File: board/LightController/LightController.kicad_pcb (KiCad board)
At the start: 2 copper layers, 79.5 x 67.1 mm, 11 parts, among them J1 Jack-DC, J2 Light bank 1, J3 Light Bank 2, J4 Light Bank 3, U1 CPC1002N, U2 AP63205WU, U3 FeatherS2

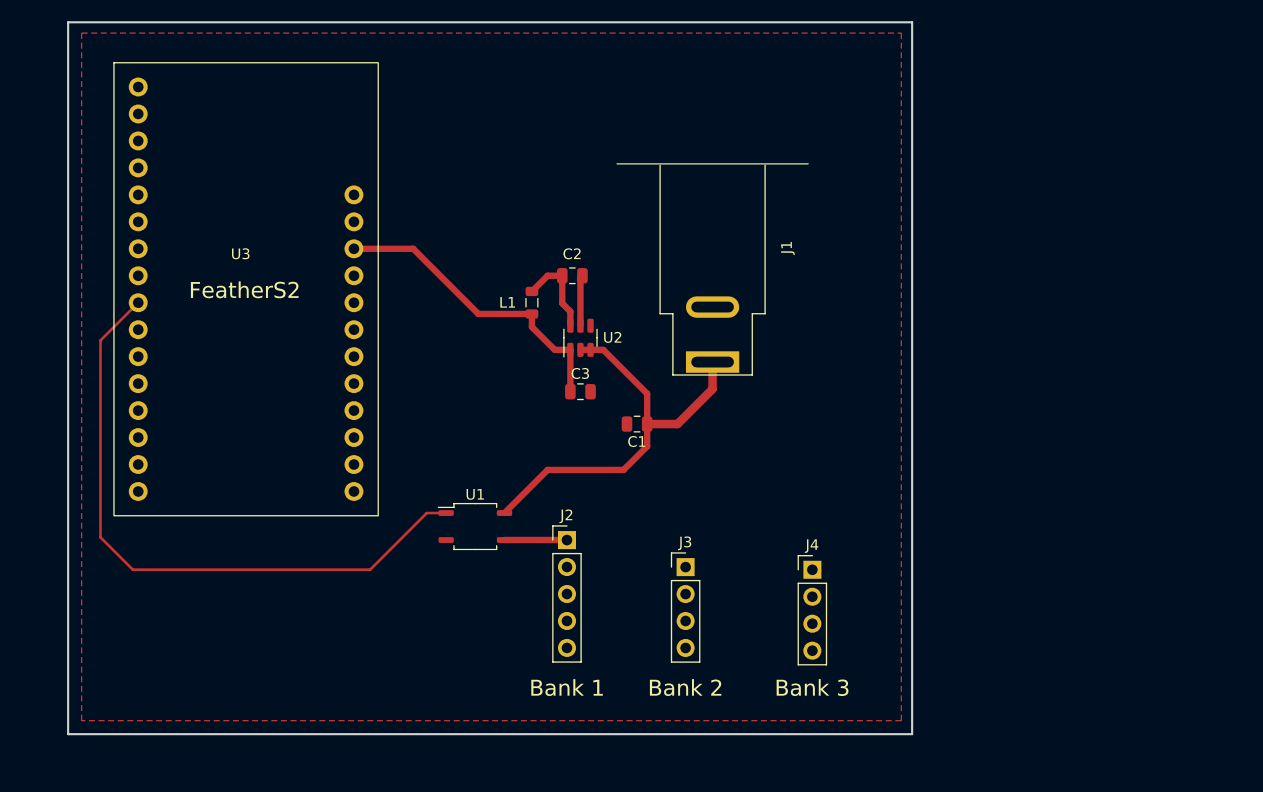
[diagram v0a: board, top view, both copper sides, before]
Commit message: Add mounting holes.
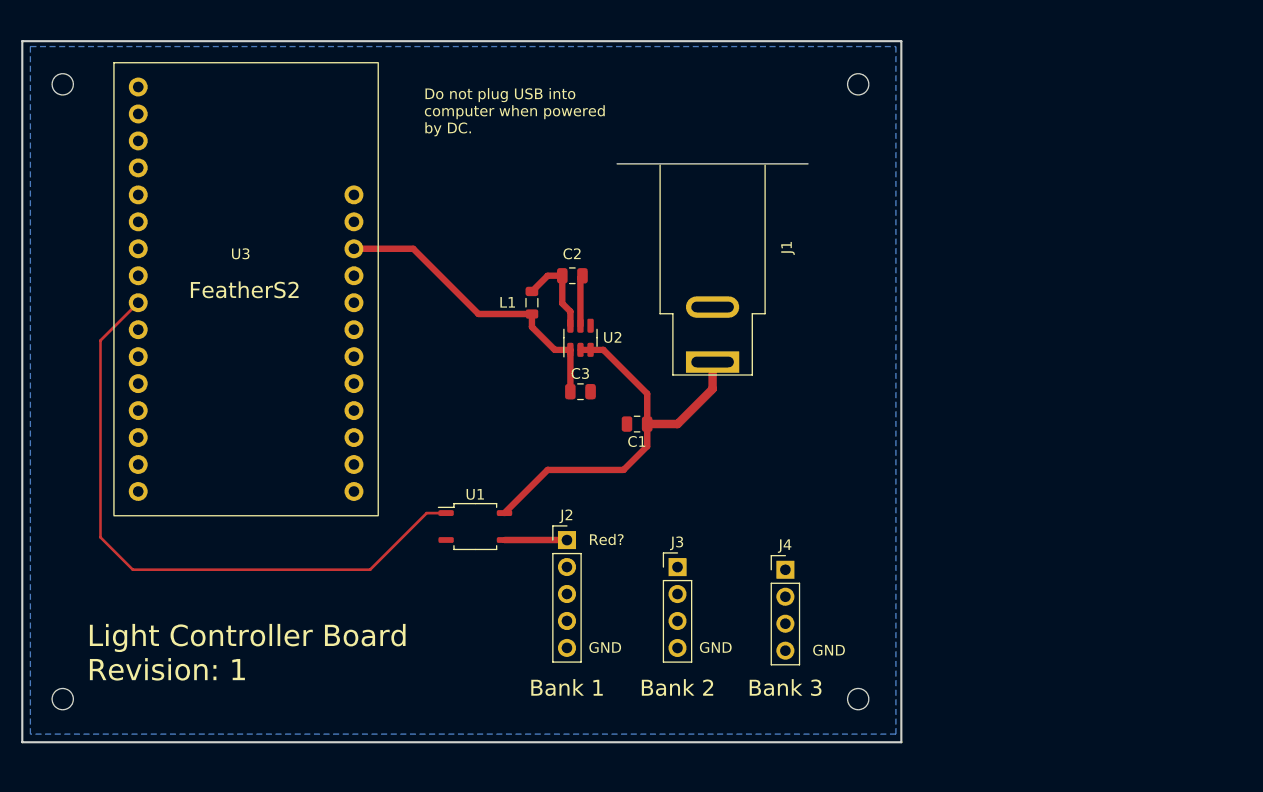
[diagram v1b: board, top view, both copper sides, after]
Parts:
- added H1: MountingHole, MountingHole:MountingHole_2mm, F.Cu at (171.7, 52.6)
- added H2: MountingHole, MountingHole:MountingHole_2mm, F.Cu at (171.7, 110.5)
- added H3: MountingHole, MountingHole:MountingHole_2mm, F.Cu at (96.8, 52.6)
- added H4: MountingHole, MountingHole:MountingHole_2mm, F.Cu at (96.8, 110.5)
- moved J4 2.54 mm to (164.8, 98.3)
- moved J3 0.76 mm to (154.7, 98.1)
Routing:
- added copper zone on B.Cu, net GND
- removed copper zone on F.Cu, net GND
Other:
- board size 79.5 x 67.1 mm -> 82.8 x 66 mm
- board text added: "Do not plug USB into computer when powered by DC."
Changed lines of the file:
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@@
       (effects (font (size 1 1) (thickness 0.15)))
     )
-    (fp_text value "100nF" (at 72.268 42.926) (layer "F.Fab")
+    (fp_text value "100nF" (at 0 -1.778) (layer "F.Fab")
       (effects (font (size 1 1) (thickness 0.15)))
     )
@@
     )
   )
+  (footprint "MountingHole:MountingHole_2mm" (layer "F.Cu")
+    (at 96.774 52.578)
+    (descr "Mounting Hole 2mm, no annular")
+    (tags "mounting hole 2mm no annular")
+    (property "Sheetfile" "LightController.kicad_sch")
+    (property "Sheetname" "")
+    (attr exclude_from_pos_files)
+    (fp_text reference "H3" (at 0 -3.2) (layer "F.SilkS") hide
+      (effects (font (size 1 1) (thickness 0.15)))
+    )
+    (fp_text value "MountingHole" (at 0 3.1) (layer "F.Fab")
+      (effects (font (size 1 1) (thickness 0.15)))
+    )
+    (fp_text user "${REFERENCE}" (at 0 0) (layer "F.Fab")
+      (effects (font (size 1 1) (thickness 0.15)))
+    )
+    (fp_circle (center 0 0) (end 2 0) (layer "Cmts.User") (width 0.15) (fill none))
+    (fp_circle (center 0 0) (end 2.25 0) (layer "F.CrtYd") (width 0.05) (fill none))
+    (pad "" np_thru_hole circle (at 0 0) (size 2 2) (drill 2) (layers *.Cu *.Mask))
+  )
   (footprint "Connector_PinHeader_2.54mm:PinHeader_1x04_P2.54mm_Vertical" (layer "F.Cu")
-    (at 167.386 98.308)
+    (at 164.846 98.308)
     (descr "Through hole straight pin header, 1x04, 2.54mm pitch, single row")
     (tags "Through hole pin header THT 1x04 2.54mm single row")
@@
       (rotate (xyz 0 0 0))
     )
+  )
+  (footprint "MountingHole:MountingHole_2mm" (layer "F.Cu")
+    (at 96.774 110.49)
+    (descr "Mounting Hole 2mm, no annular")
+    (tags "mounting hole 2mm no annular")
+    (property "Sheetfile" "LightController.kicad_sch")
+    (property "Sheetname" "")
+    (attr exclude_from_pos_files)
+    (fp_text reference "H4" (at 0 -3.2) (layer "F.SilkS") hide
+      (effects (font (size 1 1) (thickness 0.15)))
+    )
+    (fp_text value "MountingHole" (at 0 3.1) (layer "F.Fab")
+      (effects (font (size 1 1) (thickness 0.15)))
+    )
+    (fp_text user "${REFERENCE}" (at 0 0) (layer "F.Fab")
+      (effects (font (size 1 1) (thickness 0.15)))
+    )
+    (fp_circle (center 0 0) (end 2 0) (layer "Cmts.User") (width 0.15) (fill none))
+    (fp_circle (center 0 0) (end 2.25 0) (layer "F.CrtYd") (width 0.05) (fill none))
+    (pad "" np_thru_hole circle (at 0 0) (size 2 2) (drill 2) (layers *.Cu *.Mask))
   )
   (footprint "Connector_BarrelJack:BarrelJack_SwitchcraftConxall_RAPC10U_Horizontal" (layer "F.Cu")
@@
     )
   )
+  (footprint "MountingHole:MountingHole_2mm" (layer "F.Cu")
+    (at 171.704 110.49)
+    (descr "Mounting Hole 2mm, no annular")
+    (tags "mounting hole 2mm no annular")
+    (property "Sheetfile" "LightController.kicad_sch")
+    (property "Sheetname" "")
+    (attr exclude_from_pos_files)
+    (fp_text reference "H2" (at 0 -3.2) (layer "F.SilkS") hide
+      (effects (font (size 1 1) (thickness 0.15)))
+    )
+    (fp_text value "MountingHole" (at 0 3.1) (layer "F.Fab")
+      (effects (font (size 1 1) (thickness 0.15)))
+    )
+    (fp_text user "${REFERENCE}" (at 0 0) (layer "F.Fab")
+      (effects (font (size 1 1) (thickness 0.15)))
+    )
+    (fp_circle (center 0 0) (end 2 0) (layer "Cmts.User") (width 0.15) (fill none))
+    (fp_circle (center 0 0) (end 2.25 0) (layer "F.CrtYd") (width 0.05) (fill none))
+    (pad "" np_thru_hole circle (at 0 0) (size 2 2) (drill 2) (layers *.Cu *.Mask))
+  )
   (footprint "Connector_PinHeader_2.54mm:PinHeader_1x04_P2.54mm_Vertical" (layer "F.Cu")
-    (at 155.448 98.054)
+    (at 154.686 98.054)
     (descr "Through hole straight pin header, 1x04, 2.54mm pitch, single row")
     (tags "Through hole pin header THT 1x04 2.54mm single row")
@@
     )
   )
-  (gr_rect (start 97.282 46.736) (end 176.784 113.792) (layer "Edge.Cuts") (width 0.2) (fill none))
+  (footprint "MountingHole:MountingHole_2mm" (layer "F.Cu")
+    (at 171.704 52.578)
+    (descr "Mounting Hole 2mm, no annular")
+    (tags "mounting hole 2mm no annular")
+    (property "Sheetfile" "LightController.kicad_sch")
+    (property "Sheetname" "")
+    (attr exclude_from_pos_files)
+    (fp_text reference "H1" (at 0 -3.2) (layer "F.SilkS") hide
+      (effects (font (size 1 1) (thickness 0.15)))
+    )
+    (fp_text value "MountingHole" (at 0 3.1) (layer "F.Fab")
+      (effects (font (size 1 1) (thickness 0.15)))
+    )
+    (fp_text user "${REFERENCE}" (at 0 0) (layer "F.Fab")
+      (effects (font (size 1 1) (thickness 0.15)))
+    )
+    (fp_circle (center 0 0) (end 2 0) (layer "Cmts.User") (width 0.15) (fill none))
+    (fp_circle (center 0 0) (end 2.25 0) (layer "F.CrtYd") (width 0.05) (fill none))
+    (pad "" np_thru_hole circle (at 0 0) (size 2 2) (drill 2) (layers *.Cu *.Mask))
+  )
+  (gr_rect (start 92.964 48.514) (end 175.768 114.554) (layer "Edge.Cuts") (width 0.2) (fill none))
   (gr_text "Bank 1" (at 144.272 109.474) (layer "F.SilkS")
     (effects (font (size 1.5 1.5) (thickness 0.2)))
   )
-  (gr_text "Bank 3" (at 167.386 109.474) (layer "F.SilkS")
+  (gr_text "Bank 3" (at 164.846 109.474) (layer "F.SilkS")
     (effects (font (size 1.5 1.5) (thickness 0.2)))
   )
-  (gr_text "Bank 2" (at 155.448 109.474) (layer "F.SilkS")
+  (gr_text "GND" (at 146.304 105.664) (layer "F.SilkS")
+    (effects (font (size 1 1) (thickness 0.15)) (justify left))
+  )
+  (gr_text "Bank 2" (at 154.686 109.474) (layer "F.SilkS")
     (effects (font (size 1.5 1.5) (thickness 0.2)))
   )
-  (gr_text "GND" (at 146.304 105.664) (layer "Edge.Cuts")
+  (gr_text "Red?" (at 146.304 95.504) (layer "F.SilkS")
     (effects (font (size 1 1) (thickness 0.15)) (justify left))
   )
-  (gr_text "Red?" (at 146.304 95.504) (layer "Edge.Cuts")
+  (gr_text "GND" (at 167.386 105.918) (layer "F.SilkS")
     (effects (font (size 1 1) (thickness 0.15)) (justify left))
   )
-  (gr_text "GND" (at 169.418 105.918) (layer "Edge.Cuts")
+  (gr_text "Light Controller Board\nRevision: ${REVISION}" (at 99.06 106.172) (layer "F.SilkS")
+    (effects (font (size 2 2) (thickness 0.3)) (justify left))
+  )
+  (gr_text "GND" (at 156.718 105.664) (layer "F.SilkS")
     (effects (font (size 1 1) (thickness 0.15)) (justify left))
   )
-  (gr_text "Light Controller Board\nRevision: ${REVISION}" (at 102.108 106.172) (layer "Edge.Cuts")
-    (effects (font (size 2 2) (thickness 0.3)) (justify left))
-  )
-  (gr_text "GND" (at 157.226 105.664) (layer "Edge.Cuts")
+  (gr_text "Do not plug USB into\ncomputer when powered\nby DC." (at 130.81 55.118) (layer "F.SilkS")
     (effects (font (size 1 1) (thickness 0.15)) (justify left))
   )
@@
   (segment (start 132.886 92.964) (end 131.064 92.964) (width 0.25) (layer "F.Cu") (net 16))
   (segment (start 103.378 98.298) (end 100.33 95.25) (width 0.25) (layer "F.Cu") (net 16))
-  (zone (net 2) (net_name "GND") (layer "F.Cu") (hatch edge 0.508)
+  (zone (net 2) (net_name "GND") (layer "B.Cu") (hatch edge 0.508)
     (connect_pads (clearance 0.508))
     (min_thickness 0.254) (filled_areas_thickness no)
@@
     (polygon
       (pts
-        (xy 175.768 112.522)
-        (xy 98.552 112.522)
-        (xy 98.552 47.752)
-        (xy 175.768 47.752)
+        (xy 175.26 113.792)
+        (xy 93.726 113.792)
+        (xy 93.726 49.022)
+        (xy 175.26 49.022)
       )
     )

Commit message: Increase trace width and relay input resistor.
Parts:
- added R1: 3K3, Resistor_SMD:R_0805_2012Metric, F.Cu at (133.9, 100.3)
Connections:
- U1 pad 2: GND -> Net-(R1-Pad1)
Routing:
- net GND: track 0.00 -> 29.3 mm, vias 0 -> 1
- net Net-(R1-Pad1): track 0.00 -> 4.85 mm
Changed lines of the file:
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@@
   (net 40 "unconnected-(U3-Pad27)")
   (net 41 "unconnected-(U3-Pad28)")
+  (net 42 "Net-(R1-Pad1)")
+  (footprint "Resistor_SMD:R_0805_2012Metric" (layer "F.Cu")
+    (at 133.858 100.33)
+    (descr "Resistor SMD 0805 (2012 Metric), square (rectangular) end terminal, IPC_7351 nominal, (Body size source: IPC-SM-782 page 72, https://www.pcb-3d.com/wordpress/wp-content/uploads/ipc-sm-782a_amendment_1_and_2.pdf), generated with kicad-footprint-generator")
+    (tags "resistor")
+    (property "Sheetfile" "LightController.kicad_sch")
+    (property "Sheetname" "")
+    (attr smd)
+    (fp_text reference "R1" (at 0 -1.65) (layer "F.SilkS")
+      (effects (font (size 1 1) (thickness 0.15)))
+    )
+    (fp_text value "3K3" (at 0 1.65) (layer "F.Fab")
+      (effects (font (size 1 1) (thickness 0.15)))
+    )
+    (fp_text user "${REFERENCE}" (at 0 0) (layer "F.Fab")
+      (effects (font (size 0.5 0.5) (thickness 0.08)))
+    )
+    (fp_line (start -0.227064 0.735) (end 0.227064 0.735) (layer "F.SilkS") (width 0.12))
+    (fp_line (start -0.227064 -0.735) (end 0.227064 -0.735) (layer "F.SilkS") (width 0.12))
+    (fp_line (start 1.68 -0.95) (end 1.68 0.95) (layer "F.CrtYd") (width 0.05))
+    (fp_line (start -1.68 0.95) (end -1.68 -0.95) (layer "F.CrtYd") (width 0.05))
+    (fp_line (start 1.68 0.95) (end -1.68 0.95) (layer "F.CrtYd") (width 0.05))
+    (fp_line (start -1.68 -0.95) (end 1.68 -0.95) (layer "F.CrtYd") (width 0.05))
+    (fp_line (start 1 -0.625) (end 1 0.625) (layer "F.Fab") (width 0.1))
+    (fp_line (start -1 0.625) (end -1 -0.625) (layer "F.Fab") (width 0.1))
+    (fp_line (start -1 -0.625) (end 1 -0.625) (layer "F.Fab") (width 0.1))
+    (fp_line (start 1 0.625) (end -1 0.625) (layer "F.Fab") (width 0.1))
+    (pad "1" smd roundrect (at -0.9125 0) (size 1.025 1.4) (layers "F.Cu" "F.Paste" "F.Mask") (roundrect_rratio 0.243902)
+      (net 42 "Net-(R1-Pad1)") (pintype "passive"))
+    (pad "2" smd roundrect (at 0.9125 0) (size 1.025 1.4) (layers "F.Cu" "F.Paste" "F.Mask") (roundrect_rratio 0.243902)
+      (net 2 "GND") (pintype "passive"))
+    (model "${KICAD6_3DMODEL_DIR}/Resistor_SMD.3dshapes/R_0805_2012Metric.wrl"
+      (offset (xyz 0 0 0))
+      (scale (xyz 1 1 1))
+      (rotate (xyz 0 0 0))
+    )
+  )
   (footprint "cmumford:FeatherS2" (layer "F.Cu")
     (at 114.046 71.882)
@@
       (net 16 "LIGHT1_CTL") (pintype "passive"))
     (pad "2" smd roundrect (at -2.75 1.27) (size 1.45 0.55) (layers "F.Cu" "F.Paste" "F.Mask") (roundrect_rratio 0.25)
-      (net 2 "GND") (pintype "passive"))
+      (net 42 "Net-(R1-Pad1)") (pintype "passive"))
     (pad "3" smd roundrect (at 2.75 1.27) (size 1.45 0.55) (layers "F.Cu" "F.Paste" "F.Mask") (roundrect_rratio 0.25)
       (net 6 "LIGHT1_VIN") (pintype "passive"))
@@
     (effects (font (size 1 1) (thickness 0.15)) (justify left))
   )
-  (segment (start 154.686 84.582) (end 157.988 81.28) (width 0.8) (layer "F.Cu") (net 1))
-  (segment (start 157.988 81.28) (end 157.988 78.74) (width 0.8) (layer "F.Cu") (net 1))
+  (segment (start 154.686 84.582) (end 157.988 81.28) (width 2.2) (layer "F.Cu") (net 1))
+  (segment (start 157.988 81.28) (end 157.988 78.74) (width 2.2) (layer "F.Cu") (net 1))
   (segment (start 149.606 88.9) (end 151.826 86.68) (width 0.6) (layer "F.Cu") (net 1))
   (segment (start 145.542 77.5915) (end 146.492 77.5915) (width 0.6) (layer "F.Cu") (net 1))
   (segment (start 147.6955 77.5915) (end 151.826 81.722) (width 0.6) (layer "F.Cu") (net 1))
-  (segment (start 151.826 84.582) (end 154.686 84.582) (width 0.8) (layer "F.Cu") (net 1))
+  (segment (start 151.826 84.582) (end 154.686 84.582) (width 2.2) (layer "F.Cu") (net 1))
   (segment (start 151.826 81.722) (end 151.826 84.582) (width 0.6) (layer "F.Cu") (net 1))
   (segment (start 151.826 86.68) (end 151.826 84.582) (width 0.6) (layer "F.Cu") (net 1))
@@
   (segment (start 146.492 77.5915) (end 147.6955 77.5915) (width 0.6) (layer "F.Cu") (net 1))
   (segment (start 142.45 88.9) (end 149.606 88.9) (width 0.6) (layer "F.Cu") (net 1))
+  (segment (start 151.484 73.56) (end 149.7275 75.3165) (width 0.8) (layer "F.Cu") (net 2))
+  (segment (start 149.926 83.378) (end 148.844 82.296) (width 0.8) (layer "F.Cu") (net 2))
+  (segment (start 134.7705 100.33) (end 135.89 100.33) (width 0.25) (layer "F.Cu") (net 2))
+  (segment (start 149.926 84.582) (end 149.926 83.378) (width 0.8) (layer "F.Cu") (net 2))
+  (segment (start 148.082 81.534) (end 148.844 82.296) (width 0.8) (layer "F.Cu") (net 2))
+  (segment (start 146.492 81.534) (end 148.082 81.534) (width 0.8) (layer "F.Cu") (net 2))
+  (segment (start 135.89 100.33) (end 141.229 105.669) (width 0.25) (layer "F.Cu") (net 2))
+  (segment (start 141.229 105.669) (end 144.272 105.669) (width 0.25) (layer "F.Cu") (net 2))
+  (segment (start 157.988 73.56) (end 151.484 73.56) (width 0.8) (layer "F.Cu") (net 2))
+  (segment (start 149.7275 75.3165) (end 146.492 75.3165) (width 0.8) (layer "F.Cu") (net 2))
+  (via (at 148.844 82.296) (size 1.2) (drill 0.6) (layers "F.Cu" "B.Cu") (net 2))
   (segment (start 145.542 75.3165) (end 145.542 70.8) (width 0.6) (layer "F.Cu") (net 3))
   (segment (start 145.542 70.8) (end 145.73 70.612) (width 0.6) (layer "F.Cu") (net 3))
@@
   (segment (start 143.1235 77.5915) (end 144.592 77.5915) (width 0.6) (layer "F.Cu") (net 5))
   (segment (start 144.267 95.504) (end 144.272 95.509) (width 0.8) (layer "F.Cu") (net 6))
-  (segment (start 138.386 95.504) (end 144.267 95.504) (width 0.6) (layer "F.Cu") (net 6))
+  (segment (start 138.386 95.504) (end 144.267 95.504) (width 0.25) (layer "F.Cu") (net 6))
   (segment (start 100.33 95.25) (end 100.33 76.708) (width 0.25) (layer "F.Cu") (net 16))
   (segment (start 125.73 98.298) (end 103.378 98.298) (width 0.25) (layer "F.Cu") (net 16))
@@
   (segment (start 132.886 92.964) (end 131.064 92.964) (width 0.25) (layer "F.Cu") (net 16))
   (segment (start 103.378 98.298) (end 100.33 95.25) (width 0.25) (layer "F.Cu") (net 16))
+  (segment (start 132.886 100.2705) (end 132.9455 100.33) (width 0.25) (layer "F.Cu") (net 42))
+  (segment (start 132.886 95.504) (end 132.886 100.2705) (width 0.25) (layer "F.Cu") (net 42))
   (zone (net 2) (net_name "GND") (layer "B.Cu") (hatch edge 0.508)
     (connect_pads (clearance 0.508))
